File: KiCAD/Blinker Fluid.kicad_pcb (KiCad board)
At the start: 4 copper layers, 35.2 x 83.5 mm, 147 parts, among them J1 Conn_02x32_Counter_Clockwise, U1 74HCT574, U2 74HCT574, U3 74HCT574, U4 74HCT574, U5 74HCT574, U6 74HCT574, U7 74HCT574, U8 74HCT574, U9 NE555

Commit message: revised
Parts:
- C71: value 10uf -> 1uf
- R72: value 10k -> 47k

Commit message: Updated 17-02-26
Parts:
- C72: footprint Capacitor_SMD:C_0402_1005Metric_Pad0.74x0.62mm_HandSolder -> Capacitor_SMD:C_0805_2012Metric_Pad1.18x1.45mm_HandSolder
- R1, R2, R3, R4, R5, R53, R54, R55, R56, R57, R58, R59, R60, R61, R62, R63: value 330 -> 620
- R10, R11, R12, R13, R14, R15, R17, R18, R19, R20, R21, R22, R23, R24, R25, R26, R27, R49, R6, R7, R8, R9: value 680 -> 470
- R29, R30, R31, R32, R33, R34, R35, R36, R37, R38, R39, R40, R41, R42, R43, R44, R45, R46, R47, R48, R50, R51, R52: value 470 -> 820
- R71: value 1k -> 10k; footprint Resistor_SMD:R_0402_1005Metric_Pad0.72x0.64mm_HandSolder -> Resistor_SMD:R_0805_2012Metric_Pad1.20x1.40mm_HandSolder
- R72: footprint Resistor_SMD:R_0402_1005Metric_Pad0.72x0.64mm_HandSolder -> Resistor_SMD:R_0805_2012Metric_Pad1.20x1.40mm_HandSolder
- moved R71 7.25 mm to (198.7, 180.1), turned to 180 degrees
- moved C71 4.34 mm to (205.7, 179.1), turned to 90 degrees
- moved R72 3.67 mm to (202.6, 180.1)
- moved C72 3.50 mm to (202.6, 186.0), turned to 0 degrees
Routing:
- net Net-(U9-DIS): track 3.67 -> 9.10 mm
- net Net-(U9-THR): track 10.3 -> 13.5 mm
- net Net-(U9-CV): track 2.32 -> 4.69 mm
- net +5V: track 41.4 -> 42.1 mm

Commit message: Updated 25-02-26
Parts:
- C1, C2, C3, C4, C5, C6, C7, C73, C8: footprint Capacitor_SMD:C_0402_1005Metric_Pad0.74x0.62mm_HandSolder -> Capacitor_SMD:C_0603_1608Metric_Pad1.08x0.95mm_HandSolder
- D1, D2, D3, D4, D5, D53, D54, D55, D56, D57, D58, D59, D60, D61, D62, D63: footprint LED_SMD:LED_0402_1005Metric_Pad0.77x0.64mm_HandSolder -> LED_SMD:LED_0603_1608Metric_Pad1.05x0.95mm_HandSolder
- D10, D11, D12, D13, D15, D17, D18, D19, D20, D21, D22, D23, D24, D25, D26, D27, D28, D6, D7, D8, D9: value BLUE -> RED; footprint LED_SMD:LED_0402_1005Metric_Pad0.77x0.64mm_HandSolder -> LED_SMD:LED_0603_1608Metric_Pad1.05x0.95mm_HandSolder
- D14, D49: value WHITE -> RED; footprint LED_SMD:LED_0402_1005Metric_Pad0.77x0.64mm_HandSolder -> LED_SMD:LED_0603_1608Metric_Pad1.05x0.95mm_HandSolder
- D29, D30, D31, D32, D33, D34, D35, D36, D37, D38, D39, D40, D41, D42, D43, D44, D45, D46, D47, D48, D50, D51, D52: value GREEN -> RED; footprint LED_SMD:LED_0402_1005Metric_Pad0.77x0.64mm_HandSolder -> LED_SMD:LED_0603_1608Metric_Pad1.05x0.95mm_HandSolder
- R1, R2, R3, R4, R5, R53, R54, R55, R56, R57, R58, R59, R60, R61, R62, R63: value 620 -> 470; footprint Resistor_SMD:R_0402_1005Metric_Pad0.72x0.64mm_HandSolder -> Resistor_SMD:R_0603_1608Metric_Pad0.98x0.95mm_HandSolder
- R10, R11, R12, R13, R14, R15, R17, R18, R19, R20, R21, R22, R23, R24, R25, R26, R27, R28, R49, R6, R7, R8, R9: footprint Resistor_SMD:R_0402_1005Metric_Pad0.72x0.64mm_HandSolder -> Resistor_SMD:R_0603_1608Metric_Pad0.98x0.95mm_HandSolder
- R29, R30, R31, R32, R33, R34, R35, R36, R37, R38, R39, R40, R41, R42, R43, R44, R45, R46, R47, R48, R50, R51, R52: value 820 -> 470; footprint Resistor_SMD:R_0402_1005Metric_Pad0.72x0.64mm_HandSolder -> Resistor_SMD:R_0603_1608Metric_Pad0.98x0.95mm_HandSolder
- moved C8 3.95 mm to (204.2, 151.2)
- moved C1 3.93 mm to (204.1, 214.8), turned to 180 degrees
- moved C6 3.87 mm to (204.2, 199.6)
- moved C4 3.85 mm to (196.7, 151.2)
- moved C7 3.84 mm to (196.7, 166.6), turned to 0 degrees
- moved C2 3.80 mm to (196.7, 199.6)
- moved C3 3.73 mm to (204.1, 166.6), turned to 180 degrees
- moved C5 3.73 mm to (196.7, 214.8), turned to 0 degrees
- moved C73 2.93 mm to (199.1, 186.4), turned to 90 degrees
- turned R14 to 0 degrees
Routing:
- net GND: track 45.2 -> 0.00 mm, vias 49 -> 100
- net +5V: track 42.1 -> 86.4 mm, vias 28 -> 14
- net LE: track 149.3 -> 109.5 mm, vias 9 -> 0
- net Net-(D29-K): track 18.4 -> 15.2 mm
- net Net-(D14-A): track 2.83 -> 0.00 mm
- net D12: track 15.8 -> 18.5 mm
- net Net-(D25-A): track 15.1 -> 17.9 mm
- net Net-(D23-A): track 15.6 -> 13.1 mm
- net Net-(D30-K): track 20.2 -> 17.6 mm
- net Net-(D26-K): track 14.6 -> 17.1 mm
- net Net-(D31-K): track 22.2 -> 19.9 mm
- net Net-(D21-A): track 13.1 -> 15.4 mm
- net Net-(D24-A): track 17.7 -> 15.5 mm
- net Net-(D21-K): track 2.14 -> 0.00 mm
- net Net-(D20-K): track 15.8 -> 17.8 mm
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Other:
- board text added: "All 0603 LEDs on top side. Pay attention to orientation"
- board text added: "All 0603 resistors on this side should be sized for your LEDs."
- board text added: "CLOSED END IS CATHODE (-)"
- board text added: "by CRG"
- board text removed: "+"
- board text removed: "All 0402 LEDs on top side. Pay attention to orientation IS THE CATHODE (-)"
- board text removed: "All 0402 resistors on this side should be sized for your LEDs."

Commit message: Minor corrections
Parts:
- R71: value 10k -> 1k
- R72: value 47k -> 15k
- turned D1 to 0 degrees
- turned D10 to 0 degrees
- turned D11 to 0 degrees
- turned D12 to 0 degrees
- turned D13 to 0 degrees
- turned D14 to 0 degrees
- turned D15 to 0 degrees
- turned D17 to 0 degrees
- turned D18 to 0 degrees
- turned D19 to 0 degrees
- turned D2 to 0 degrees
- turned D20 to 0 degrees
- turned D21 to 0 degrees
- turned D22 to 0 degrees
- turned D23 to 0 degrees
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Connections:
- R1 pad 2: Net-(D1-A) -> Net-(D1-K)
- R10 pad 2: Net-(D10-K) -> Net-(D10-A)
- R11 pad 2: Net-(D11-K) -> Net-(D11-A)
- R12 pad 2: Net-(D12-K) -> Net-(D12-A)
- R13 pad 2: Net-(D13-K) -> Net-(D13-A)
- R15 pad 2: Net-(D15-A) -> Net-(D15-K)
- R17 pad 2: Net-(D17-K) -> Net-(D17-A)
- R18 pad 2: Net-(D18-K) -> Net-(D18-A)
- R19 pad 2: Net-(D19-K) -> Net-(D19-A)
- R2 pad 2: Net-(D2-A) -> Net-(D2-K)
- R20 pad 2: Net-(D20-A) -> Net-(D20-K)
- R21 pad 2: Net-(D21-K) -> Net-(D21-A)
- R22 pad 2: Net-(D22-K) -> Net-(D22-A)
- R23 pad 2: Net-(D23-K) -> Net-(D23-A)
- R24 pad 2: Net-(D24-K) -> Net-(D24-A)
- R25 pad 2: Net-(D25-K) -> Net-(D25-A)
- R26 pad 2: Net-(D26-A) -> Net-(D26-K)
- R27 pad 2: Net-(D27-A) -> Net-(D27-K)
- R28 pad 2: Net-(D28-A) -> Net-(D28-K)
- R29 pad 2: Net-(D29-A) -> Net-(D29-K)
- R3 pad 2: Net-(D3-A) -> Net-(D3-K)
- R30 pad 2: Net-(D30-A) -> Net-(D30-K)
- R31 pad 2: Net-(D31-A) -> Net-(D31-K)
- R32 pad 2: Net-(D32-A) -> Net-(D32-K)
- R33 pad 2: Net-(D33-A) -> Net-(D33-K)
- R34 pad 2: Net-(D34-A) -> Net-(D34-K)
- R35 pad 2: Net-(D35-A) -> Net-(D35-K)
- R36 pad 2: Net-(D36-A) -> Net-(D36-K)
- R37 pad 2: Net-(D37-A) -> Net-(D37-K)
- R38 pad 2: Net-(D38-A) -> Net-(D38-K)
- R39 pad 2: Net-(D39-A) -> Net-(D39-K)
- R4 pad 2: Net-(D4-A) -> Net-(D4-K)
- R40 pad 2: Net-(D40-A) -> Net-(D40-K)
- R41 pad 2: Net-(D41-A) -> Net-(D41-K)
- R42 pad 2: Net-(D42-A) -> Net-(D42-K)
- R43 pad 2: Net-(D43-A) -> Net-(D43-K)
- R44 pad 2: Net-(D44-A) -> Net-(D44-K)
- R45 pad 2: Net-(D45-A) -> Net-(D45-K)
- R46 pad 2: Net-(D46-A) -> Net-(D46-K)
- R47 pad 2: Net-(D47-A) -> Net-(D47-K)
- R48 pad 2: Net-(D48-A) -> Net-(D48-K)
- R5 pad 2: Net-(D5-A) -> Net-(D5-K)
- R50 pad 2: Net-(D50-A) -> Net-(D50-K)
- R51 pad 2: Net-(D51-A) -> Net-(D51-K)
- R52 pad 2: Net-(D52-A) -> Net-(D52-K)
- R53 pad 2: Net-(D53-A) -> Net-(D53-K)
- R54 pad 2: Net-(D54-A) -> Net-(D54-K)
- R55 pad 2: Net-(D55-A) -> Net-(D55-K)
- R56 pad 2: Net-(D56-A) -> Net-(D56-K)
- R57 pad 2: Net-(D57-A) -> Net-(D57-K)
- R58 pad 2: Net-(D58-A) -> Net-(D58-K)
- R59 pad 2: Net-(D59-A) -> Net-(D59-K)
- R6 pad 2: Net-(D6-K) -> Net-(D6-A)
- R60 pad 2: Net-(D60-A) -> Net-(D60-K)
- R61 pad 2: Net-(D61-A) -> Net-(D61-K)
- R62 pad 2: Net-(D62-A) -> Net-(D62-K)
- R63 pad 2: Net-(D63-A) -> Net-(D63-K)
- R7 pad 2: Net-(D7-K) -> Net-(D7-A)
- R8 pad 2: Net-(D8-K) -> Net-(D8-A)
- R9 pad 2: Net-(D9-K) -> Net-(D9-A)
- U1 pad 12: Net-(D1-K) -> Net-(D1-A)
- U1 pad 13: Net-(D2-K) -> Net-(D2-A)
- U1 pad 14: Net-(D3-K) -> Net-(D3-A)
- U1 pad 15: Net-(D4-K) -> Net-(D4-A)
- U1 pad 16: Net-(D5-K) -> Net-(D5-A)
- U1 pad 17: Net-(D6-A) -> Net-(D6-K)
- U1 pad 18: Net-(D7-A) -> Net-(D7-K)
- U1 pad 19: Net-(D8-A) -> Net-(D8-K)
- U2 pad 12: Net-(D9-A) -> Net-(D9-K)
- U2 pad 13: Net-(D10-A) -> Net-(D10-K)
- U2 pad 14: Net-(D11-A) -> Net-(D11-K)
- U2 pad 15: Net-(D12-A) -> Net-(D12-K)
- U2 pad 16: Net-(D13-A) -> Net-(D13-K)
- U2 pad 18: Net-(D15-K) -> Net-(D15-A)
- U3 pad 12: Net-(D17-A) -> Net-(D17-K)
- U3 pad 13: Net-(D18-A) -> Net-(D18-K)
- U3 pad 14: Net-(D19-A) -> Net-(D19-K)
- U3 pad 15: Net-(D20-K) -> Net-(D20-A)
- U3 pad 16: Net-(D21-A) -> Net-(D21-K)
- U3 pad 17: Net-(D22-A) -> Net-(D22-K)
- U3 pad 18: Net-(D23-A) -> Net-(D23-K)
- U3 pad 19: Net-(D24-A) -> Net-(D24-K)
- U4 pad 12: Net-(D25-A) -> Net-(D25-K)
- U4 pad 13: Net-(D26-K) -> Net-(D26-A)
- U4 pad 14: Net-(D27-K) -> Net-(D27-A)
- U4 pad 15: Net-(D28-K) -> Net-(D28-A)
- U4 pad 16: Net-(D29-K) -> Net-(D29-A)
- U4 pad 17: Net-(D30-K) -> Net-(D30-A)
- U4 pad 18: Net-(D31-K) -> Net-(D31-A)
- U4 pad 19: Net-(D32-K) -> Net-(D32-A)
- U5 pad 12: Net-(D33-K) -> Net-(D33-A)
- U5 pad 13: Net-(D34-K) -> Net-(D34-A)
- U5 pad 14: Net-(D35-K) -> Net-(D35-A)
- U5 pad 15: Net-(D36-K) -> Net-(D36-A)
- U5 pad 16: Net-(D37-K) -> Net-(D37-A)
- U5 pad 17: Net-(D38-K) -> Net-(D38-A)
- U5 pad 18: Net-(D39-K) -> Net-(D39-A)
- U5 pad 19: Net-(D40-K) -> Net-(D40-A)
- U6 pad 12: Net-(D41-K) -> Net-(D41-A)
- U6 pad 13: Net-(D42-K) -> Net-(D42-A)
- U6 pad 14: Net-(D43-K) -> Net-(D43-A)
- U6 pad 15: Net-(D44-K) -> Net-(D44-A)
- U6 pad 16: Net-(D45-K) -> Net-(D45-A)
- U6 pad 17: Net-(D46-K) -> Net-(D46-A)
- U6 pad 18: Net-(D47-K) -> Net-(D47-A)
- U6 pad 19: Net-(D48-K) -> Net-(D48-A)
- U7 pad 13: Net-(D50-K) -> Net-(D50-A)
- U7 pad 14: Net-(D51-K) -> Net-(D51-A)
- U7 pad 15: Net-(D52-K) -> Net-(D52-A)
- U7 pad 17: Net-(D53-K) -> Net-(D53-A)
- U7 pad 18: Net-(D54-K) -> Net-(D54-A)
- U7 pad 19: Net-(D55-K) -> Net-(D55-A)
- U8 pad 12: Net-(D56-K) -> Net-(D56-A)
- U8 pad 13: Net-(D57-K) -> Net-(D57-A)
- U8 pad 14: Net-(D58-K) -> Net-(D58-A)
- U8 pad 15: Net-(D59-K) -> Net-(D59-A)
- U8 pad 16: Net-(D60-K) -> Net-(D60-A)
- U8 pad 17: Net-(D61-K) -> Net-(D61-A)
- U8 pad 18: Net-(D62-K) -> Net-(D62-A)
- U8 pad 19: Net-(D63-K) -> Net-(D63-A)
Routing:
- net Net-(D48-K): track 30.3 -> 0.00 mm, vias 0 -> 1
- net Net-(D48-A): track 0.00 -> 30.3 mm, vias 1 -> 0
- net Net-(D47-K): track 28.2 -> 0.00 mm, vias 0 -> 1
- net Net-(D47-A): track 0.00 -> 28.2 mm, vias 1 -> 0
- net Net-(D15-K): track 28.0 -> 0.00 mm, vias 0 -> 1
- net Net-(D15-A): track 0.00 -> 28.0 mm, vias 1 -> 0
- net Net-(D46-K): track 26.1 -> 0.00 mm, vias 0 -> 1
- net Net-(D46-A): track 0.00 -> 26.1 mm, vias 1 -> 0
- net Net-(D40-K): track 25.9 -> 0.00 mm, vias 0 -> 1
- net Net-(D40-A): track 0.00 -> 25.9 mm, vias 1 -> 0
- net Net-(D8-K): track 0.00 -> 25.3 mm, vias 1 -> 0
- net Net-(D8-A): track 25.3 -> 0.00 mm, vias 0 -> 1
- net Net-(D45-K): track 24.2 -> 0.00 mm, vias 0 -> 1
- net Net-(D45-A): track 0.00 -> 24.2 mm, vias 1 -> 0
- net Net-(D13-K): track 0.00 -> 23.8 mm, vias 1 -> 0
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
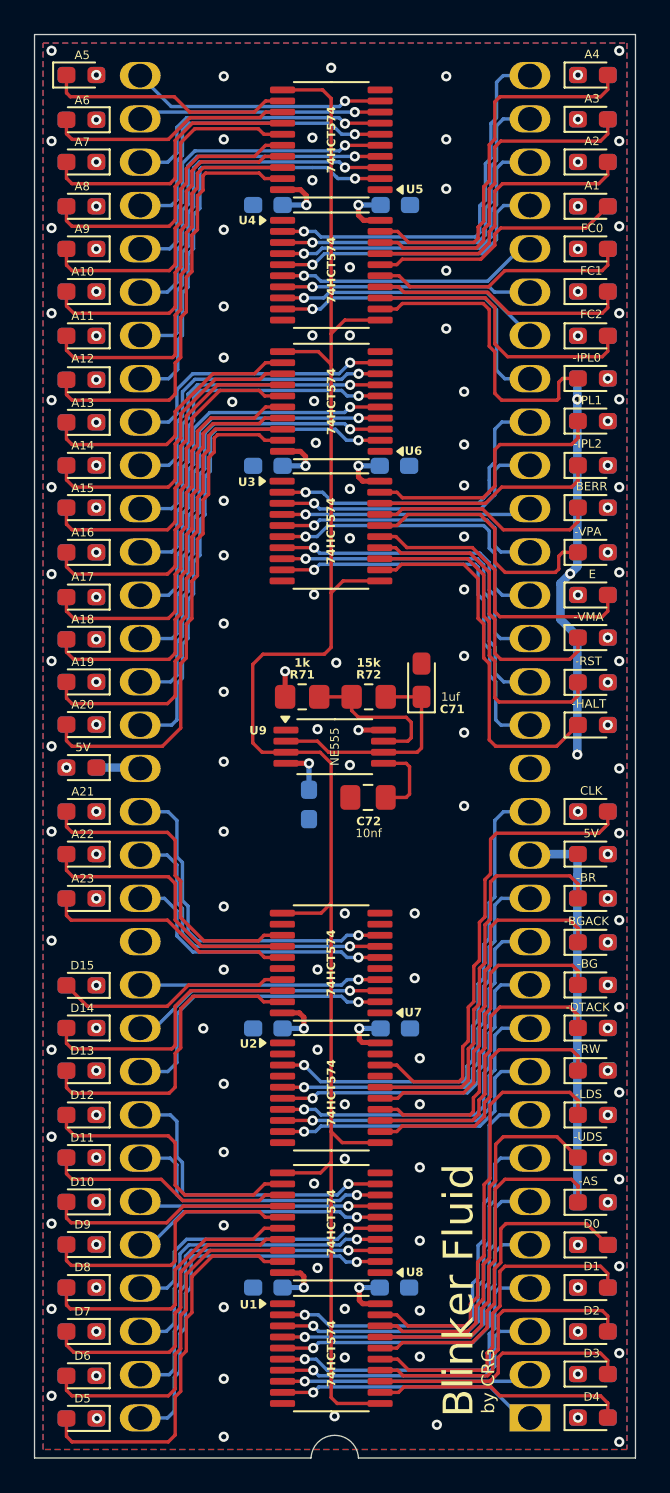
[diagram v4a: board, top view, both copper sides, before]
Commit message: PCB revised to clear short
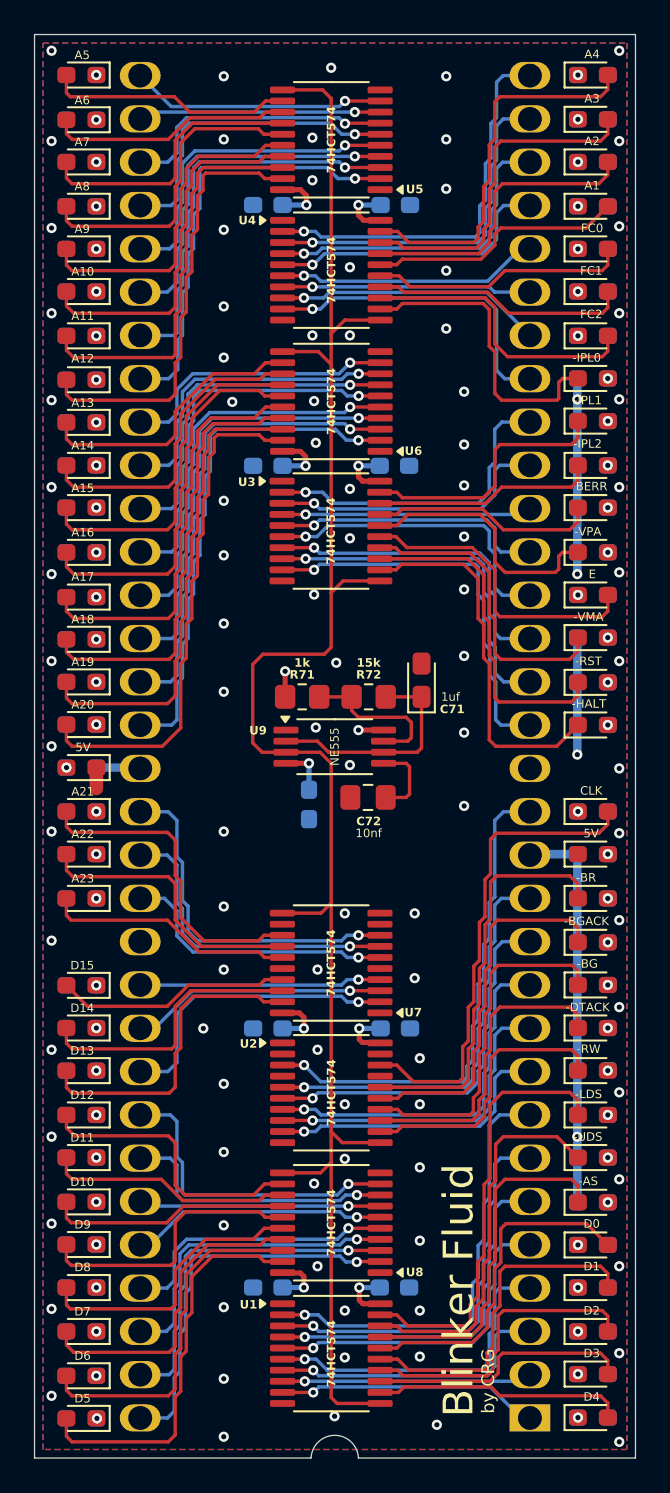
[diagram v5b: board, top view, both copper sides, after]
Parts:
- turned D33 to 180 degrees
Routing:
- net +5V: track 81.0 -> 318.5 mm, vias 14 -> 15
- net Net-(D33-K): track 14.5 -> 0.00 mm, vias 0 -> 1
- net Net-(D33-A): track 0.00 -> 14.5 mm, vias 1 -> 0
- net GND: track 0.00 -> 1.22 mm, vias 100 -> 99
- removed copper zone on In2.Cu, net +5V
